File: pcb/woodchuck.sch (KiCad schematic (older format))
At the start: 5 parts, among them IC1 ADP3335, P1 CONN_01X02

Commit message: Begin routing GPS
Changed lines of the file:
@@
 F0 "GPS" 60
 F1 "GPS_Ublox.sch" 60
+F2 "GPS_FROM_MCU" I R 3600 1500 60
+F3 "GPS_TO_MCU" O R 3600 1600 60
 $EndSheet
 $Sheet
@@
 	1    0    0    -1
 $EndComp
-Wire Notes Line
-	3850 7250 6450 7250
-Wire Notes Line
-	6450 7250 6450 5900
-Wire Notes Line
-	6450 5900 3850 5900
-Wire Wire Line
-	4200 6550 4850 6550
-Wire Notes Line
-	3850 5900 3850 7250
-Wire Wire Line
-	5550 6450 5700 6450
-Wire Wire Line
-	5700 6450 5700 6650
-Wire Wire Line
-	5700 6650 5550 6650
-Connection ~ 5700 6550
-Wire Wire Line
-	5550 6750 5650 6750
-Wire Wire Line
-	5650 6750 5650 6850
-Wire Wire Line
-	5650 6850 5850 6850
-Connection ~ 5850 6550
-Wire Wire Line
-	4850 6750 4750 6750
-Wire Wire Line
-	4750 6750 4750 6850
-Wire Wire Line
-	4750 6850 4200 6850
-Wire Wire Line
-	5850 6550 5850 6450
-Wire Wire Line
-	5550 6550 6100 6550
-Wire Wire Line
-	4750 6650 4850 6650
-Wire Wire Line
-	4750 6450 4750 6650
-Connection ~ 4750 6550
 $Comp
 L GND #PWR4
@@
 	-1   0    0    1
 $EndComp
-Wire Wire Line
-	4200 6750 4200 6900
-Wire Wire Line
-	4200 6650 4200 6550
 $Comp
 L +BATT #PWR1
@@
 	1    0    0    -1
 $EndComp
-Wire Wire Line
-	4750 6450 4850 6450
-Connection ~ 4200 6850
 $Comp
 L +3V3 #PWR3
@@
 	1    0    0    -1
 $EndComp
+Wire Notes Line
+	3850 7250 6450 7250
+Wire Notes Line
+	6450 7250 6450 5900
+Wire Notes Line
+	6450 5900 3850 5900
+Wire Wire Line
+	4200 6550 4850 6550
+Wire Notes Line
+	3850 5900 3850 7250
+Wire Wire Line
+	5550 6450 5700 6450
+Wire Wire Line
+	5700 6450 5700 6650
+Wire Wire Line
+	5700 6650 5550 6650
+Connection ~ 5700 6550
+Wire Wire Line
+	5550 6750 5650 6750
+Wire Wire Line
+	5650 6750 5650 6850
+Wire Wire Line
+	5650 6850 5850 6850
+Connection ~ 5850 6550
+Wire Wire Line
+	4850 6750 4750 6750
+Wire Wire Line
+	4750 6750 4750 6850
+Wire Wire Line
+	4750 6850 4200 6850
+Wire Wire Line
+	5850 6550 5850 6450
+Wire Wire Line
+	5550 6550 6100 6550
+Wire Wire Line
+	4750 6650 4850 6650
+Wire Wire Line
+	4750 6450 4750 6650
+Connection ~ 4750 6550
+Wire Wire Line
+	4200 6750 4200 6900
+Wire Wire Line
+	4200 6650 4200 6550
+Wire Wire Line
+	4750 6450 4850 6450
+Connection ~ 4200 6850
 Connection ~ 4400 6850
 Connection ~ 4400 6550

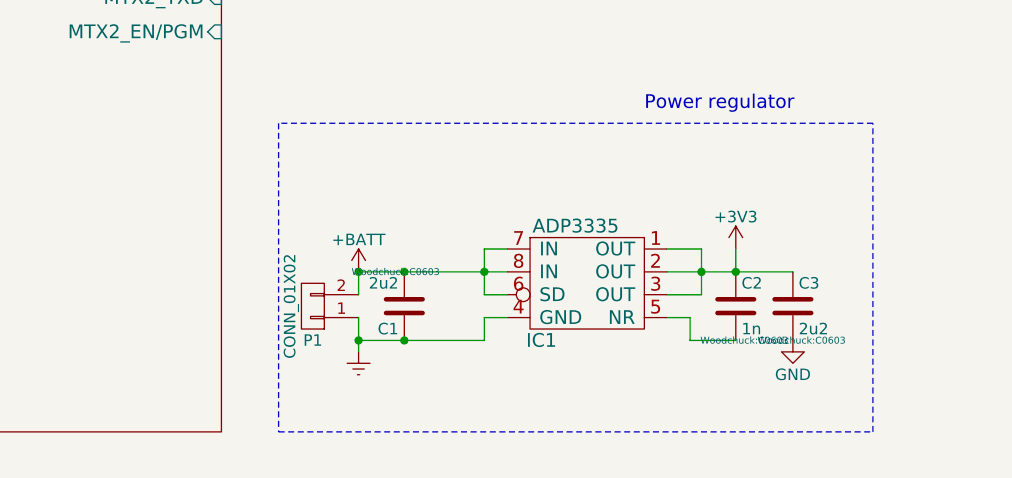
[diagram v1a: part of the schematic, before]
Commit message: Generated net list (only two footprints remaining), added a few footprints, started rough estimate of PCB size
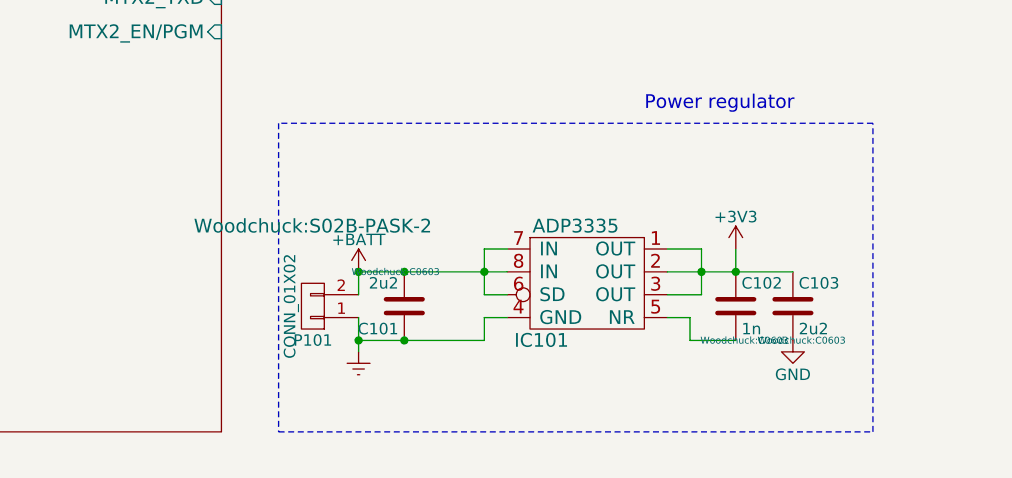
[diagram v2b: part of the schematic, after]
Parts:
- P101: renamed from P1; footprint (none) -> Woodchuck:S02B-PASK-2
- renumbered C1 to C101, C2 to C102, C3 to C103, IC1 to IC101
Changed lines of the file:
@@
 $EndSheet
 $Comp
-L ADP3335 IC1
+L ADP3335 IC101
 U 1 1 565E3BA6
 P 5200 6550
-F 0 "IC1" H 5000 6250 60  0000 C CNN
+F 0 "IC101" H 5000 6250 60  0000 C CNN
 F 1 "ADP3335" H 5150 6750 60  0000 C CNN
 F 2 "" H 5600 6150 60  0000 C CNN
@@
 Power regulator
 $Comp
-L C C2
+L C C102
 U 1 1 565E4A3A
 P 5850 6700
-F 0 "C2" H 5875 6800 50  0000 L CNN
+F 0 "C102" H 5875 6800 50  0000 L CNN
 F 1 "1n" H 5875 6600 50  0000 L CNN
 F 2 "Woodchuck:C0603" H 5888 6550 30  0000 C CNN
@@
 $EndComp
 $Comp
-L Earth #PWR2
+L Earth #PWR01
 U 1 1 565E4C8C
 P 4200 6900
-F 0 "#PWR2" H 4200 6650 50  0001 C CNN
+F 0 "#PWR01" H 4200 6650 50  0001 C CNN
 F 1 "Earth" H 4200 6750 50  0001 C CNN
 F 2 "" H 4200 6900 60  0000 C CNN
@@
 $EndComp
 $Comp
-L C C3
+L C C103
 U 1 1 565E50FD
 P 6100 6700
-F 0 "C3" H 6125 6800 50  0000 L CNN
+F 0 "C103" H 6125 6800 50  0000 L CNN
 F 1 "2u2" H 6125 6600 50  0000 L CNN
 F 2 "Woodchuck:C0603" H 6138 6550 30  0000 C CNN
@@
 $EndComp
 $Comp
-L GND #PWR4
+L GND #PWR02
 U 1 1 565E565A
 P 6100 6850
-F 0 "#PWR4" H 6100 6600 50  0001 C CNN
+F 0 "#PWR02" H 6100 6600 50  0001 C CNN
 F 1 "GND" H 6100 6700 50  0000 C CNN
 F 2 "" H 6100 6850 60  0000 C CNN
@@
 $EndComp
 $Comp
-L C C1
+L C C101
 U 1 1 565E43E2
 P 4400 6700
-F 0 "C1" H 4425 6800 50  0000 L CNN
+F 0 "C101" H 4425 6800 50  0000 L CNN
 F 1 "2u2" H 4425 6600 50  0000 L CNN
 F 2 "Woodchuck:C0603" H 4438 6550 30  0000 C CNN
@@
 $EndComp
 $Comp
-L CONN_01X02 P1
+L CONN_01X02 P101
 U 1 1 565EBDD9
 P 4000 6700
-F 0 "P1" H 4000 6850 50  0000 C CNN
+F 0 "P101" H 4000 6850 50  0000 C CNN
 F 1 "CONN_01X02" V 4100 6700 50  0000 C CNN
-F 2 "" H 4000 6700 60  0000 C CNN
+F 2 "Woodchuck:S02B-PASK-2" H 4000 6350 60  0000 C CNN
 F 3 "" H 4000 6700 60  0000 C CNN
 	1    4000 6700
@@
 $EndComp
 $Comp
-L +BATT #PWR1
+L +BATT #PWR03
 U 1 1 565EBEEE
 P 4200 6550
-F 0 "#PWR1" H 4200 6400 50  0001 C CNN
+F 0 "#PWR03" H 4200 6400 50  0001 C CNN
 F 1 "+BATT" H 4200 6690 50  0000 C CNN
 F 2 "" H 4200 6550 60  0000 C CNN
@@
 $EndComp
 $Comp
-L +3V3 #PWR3
+L +3V3 #PWR04
 U 1 1 565EC163
 P 5850 6450
-F 0 "#PWR3" H 5850 6300 50  0001 C CNN
+F 0 "#PWR04" H 5850 6300 50  0001 C CNN
 F 1 "+3V3" H 5850 6590 50  0000 C CNN
 F 2 "" H 5850 6450 60  0000 C CNN

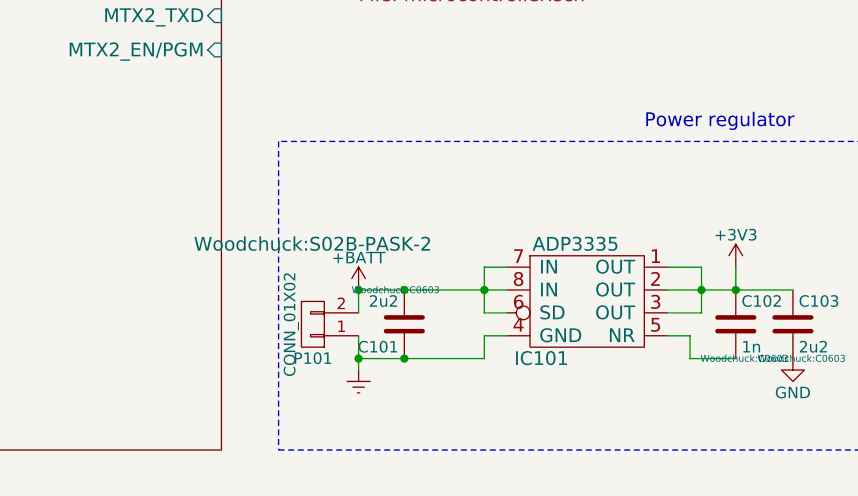
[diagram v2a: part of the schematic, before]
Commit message: Added a footprint and changed footprints for resistors to the 0603 SMD footprint.
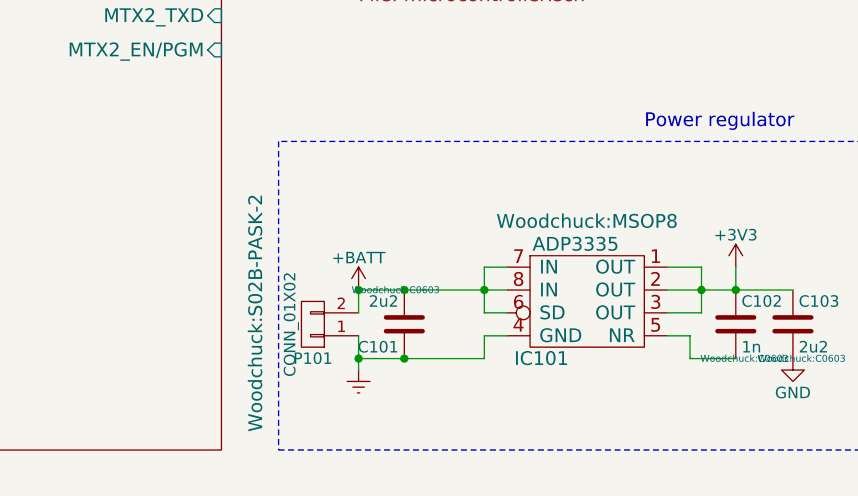
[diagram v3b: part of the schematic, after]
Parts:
- IC101: footprint (none) -> Woodchuck:MSOP8
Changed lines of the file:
@@
 F 0 "IC101" H 5000 6250 60  0000 C CNN
 F 1 "ADP3335" H 5150 6750 60  0000 C CNN
-F 2 "" H 5600 6150 60  0000 C CNN
+F 2 "Woodchuck:MSOP8" H 5200 6850 60  0000 C CNN
 F 3 "" H 5600 6150 60  0000 C CNN
 	1    5200 6550
@@
 F 0 "P101" H 4000 6850 50  0000 C CNN
 F 1 "CONN_01X02" V 4100 6700 50  0000 C CNN
-F 2 "Woodchuck:S02B-PASK-2" H 4000 6350 60  0000 C CNN
+F 2 "Woodchuck:S02B-PASK-2" V 4250 6650 60  0000 C CNN
 F 3 "" H 4000 6700 60  0000 C CNN
 	1    4000 6700

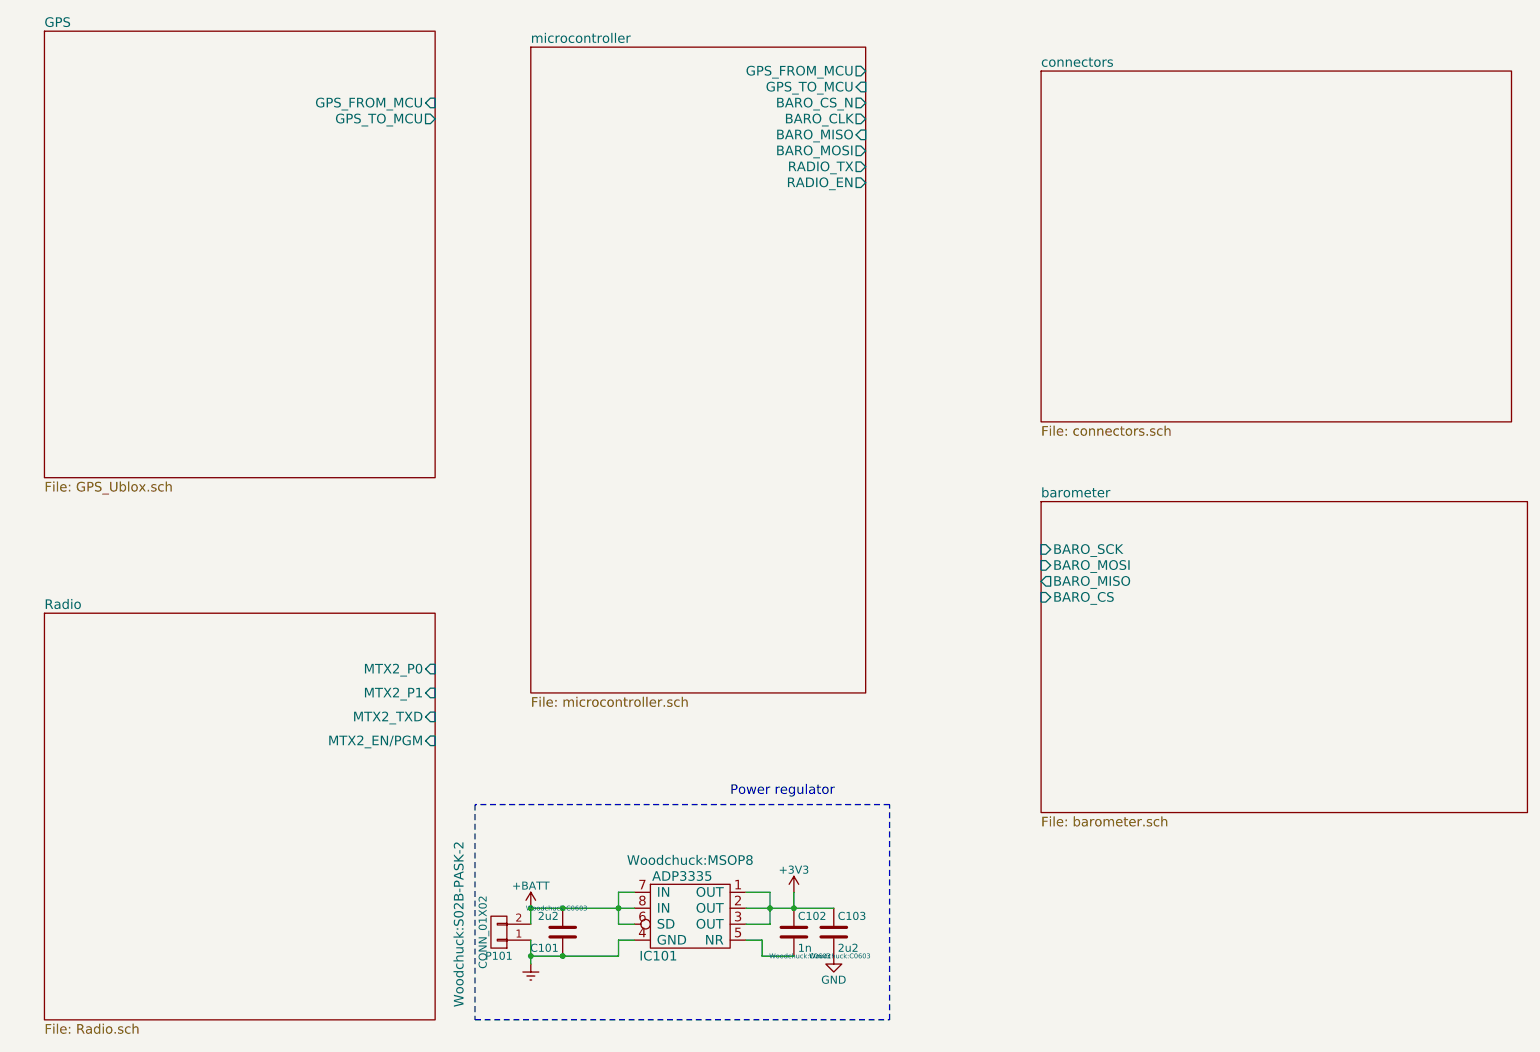
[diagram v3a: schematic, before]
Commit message: Connect hierarchical pins
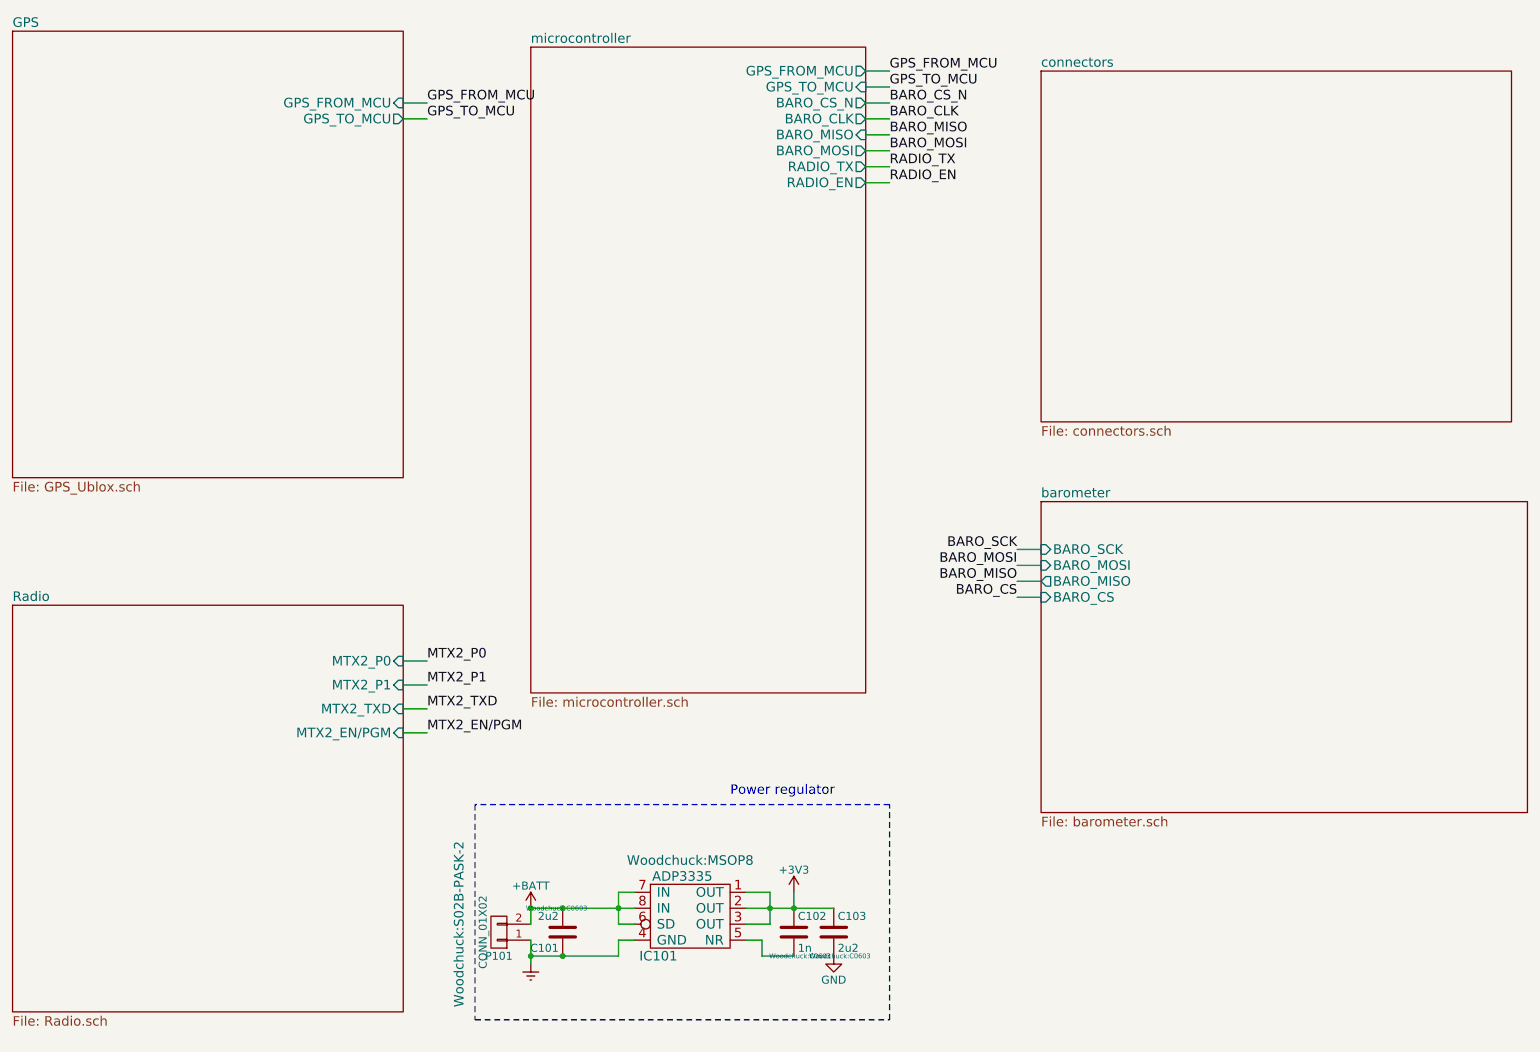
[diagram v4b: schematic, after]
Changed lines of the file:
@@
 $EndDescr
 $Sheet
-S 1150 1050 2450 2800
+S 950  1050 2450 2800
 U 56574088
 F0 "GPS" 60
 F1 "GPS_Ublox.sch" 60
-F2 "GPS_FROM_MCU" I R 3600 1500 60
-F3 "GPS_TO_MCU" O R 3600 1600 60
-$EndSheet
-$Sheet
-S 1150 4700 2450 2550
+F2 "GPS_FROM_MCU" I R 3400 1500 60
+F3 "GPS_TO_MCU" O R 3400 1600 60
+$EndSheet
+$Sheet
+S 950  4650 2450 2550
 U 5657408B
 F0 "Radio" 60
 F1 "Radio.sch" 60
-F2 "MTX2_P0" I R 3600 5050 60
-F3 "MTX2_P1" I R 3600 5200 60
-F4 "MTX2_TXD" I R 3600 5350 60
-F5 "MTX2_EN/PGM" I R 3600 5500 60
+F2 "MTX2_P0" I R 3400 5000 60
+F3 "MTX2_P1" I R 3400 5150 60
+F4 "MTX2_TXD" I R 3400 5300 60
+F5 "MTX2_EN/PGM" I R 3400 5450 60
 $EndSheet
 $Sheet
@@
 Connection ~ 4400 6550
 Connection ~ 4200 6550
+Wire Wire Line
+	3400 1500 3550 1500
+Wire Wire Line
+	3400 1600 3550 1600
+Text Label 3550 1500 0    60   ~ 0
+GPS_FROM_MCU
+Text Label 3550 1600 0    60   ~ 0
+GPS_TO_MCU
+Wire Wire Line
+	6300 1300 6450 1300
+Wire Wire Line
+	6300 1400 6450 1400
+Wire Wire Line
+	6300 1500 6450 1500
+Wire Wire Line
+	6300 1600 6450 1600
+Wire Wire Line
+	6300 1700 6450 1700
+Wire Wire Line
+	6300 1800 6450 1800
+Wire Wire Line
+	6300 1900 6450 1900
+Wire Wire Line
+	6300 2000 6450 2000
+Text Label 6450 1300 0    60   ~ 0
+GPS_FROM_MCU
+Text Label 6450 1400 0    60   ~ 0
+GPS_TO_MCU
+Text Label 6450 1500 0    60   ~ 0
+BARO_CS_N
+Text Label 6450 1600 0    60   ~ 0
+BARO_CLK
+Text Label 6450 1700 0    60   ~ 0
+BARO_MISO
+Text Label 6450 1800 0    60   ~ 0
+BARO_MOSI
+Text Label 6450 1900 0    60   ~ 0
+RADIO_TX
+Text Label 6450 2000 0    60   ~ 0
+RADIO_EN
+Wire Wire Line
+	3400 5000 3550 5000
+Wire Wire Line
+	3400 5150 3550 5150
+Wire Wire Line
+	3400 5300 3550 5300
+Wire Wire Line
+	3400 5450 3550 5450
+Text Label 3550 5000 0    60   ~ 0
+MTX2_P0
+Text Label 3550 5150 0    60   ~ 0
+MTX2_P1
+Text Label 3550 5300 0    60   ~ 0
+MTX2_TXD
+Text Label 3550 5450 0    60   ~ 0
+MTX2_EN/PGM
+Wire Wire Line
+	7400 4300 7250 4300
+Wire Wire Line
+	7400 4400 7250 4400
+Wire Wire Line
+	7400 4500 7250 4500
+Wire Wire Line
+	7400 4600 7250 4600
+Text Label 7250 4300 2    60   ~ 0
+BARO_SCK
+Text Label 7250 4400 2    60   ~ 0
+BARO_MOSI
+Text Label 7250 4500 2    60   ~ 0
+BARO_MISO
+Text Label 7250 4600 2    60   ~ 0
+BARO_CS
 $EndSCHEMATC

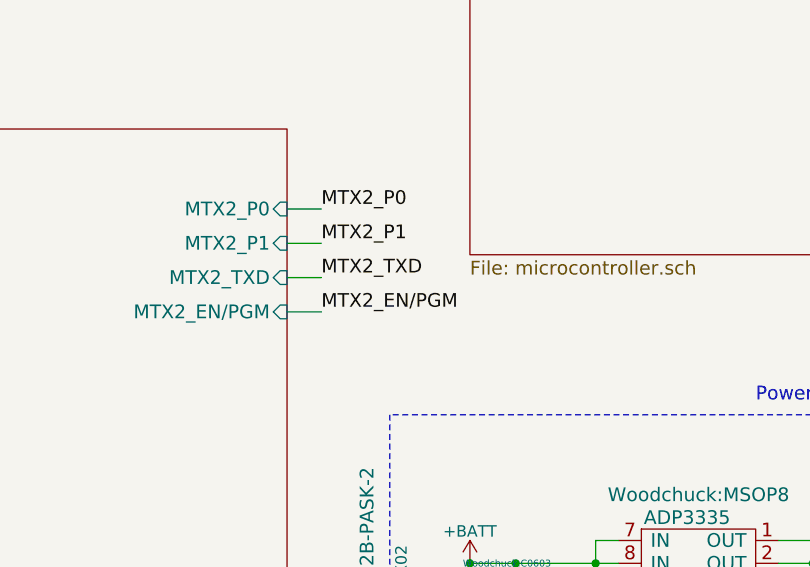
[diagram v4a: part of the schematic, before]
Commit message: Fix LED circuit and radio tx/rx labels, start LED driver code
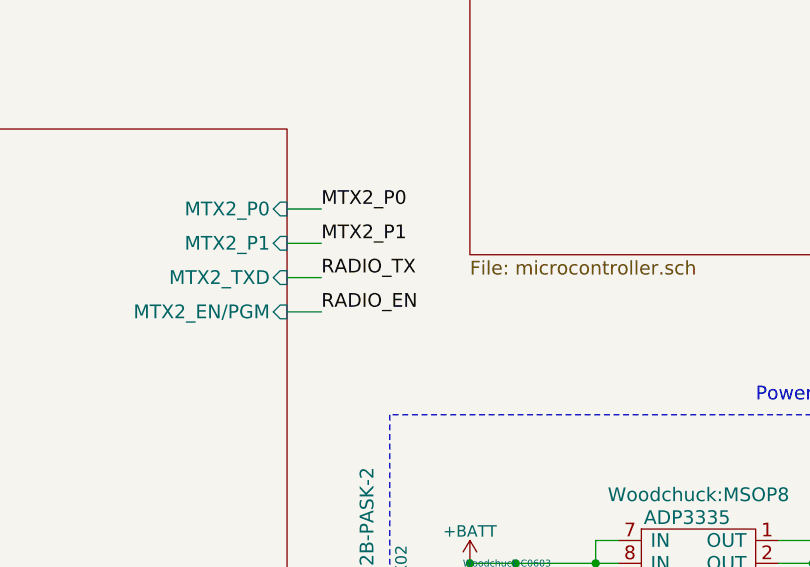
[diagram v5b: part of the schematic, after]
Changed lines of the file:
@@
 MTX2_P1
 Text Label 3550 5300 0    60   ~ 0
-MTX2_TXD
+RADIO_TX
 Text Label 3550 5450 0    60   ~ 0
-MTX2_EN/PGM
+RADIO_EN
 Wire Wire Line
 	7400 4300 7250 4300
